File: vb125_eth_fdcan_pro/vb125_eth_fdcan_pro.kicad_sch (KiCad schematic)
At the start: 0 parts

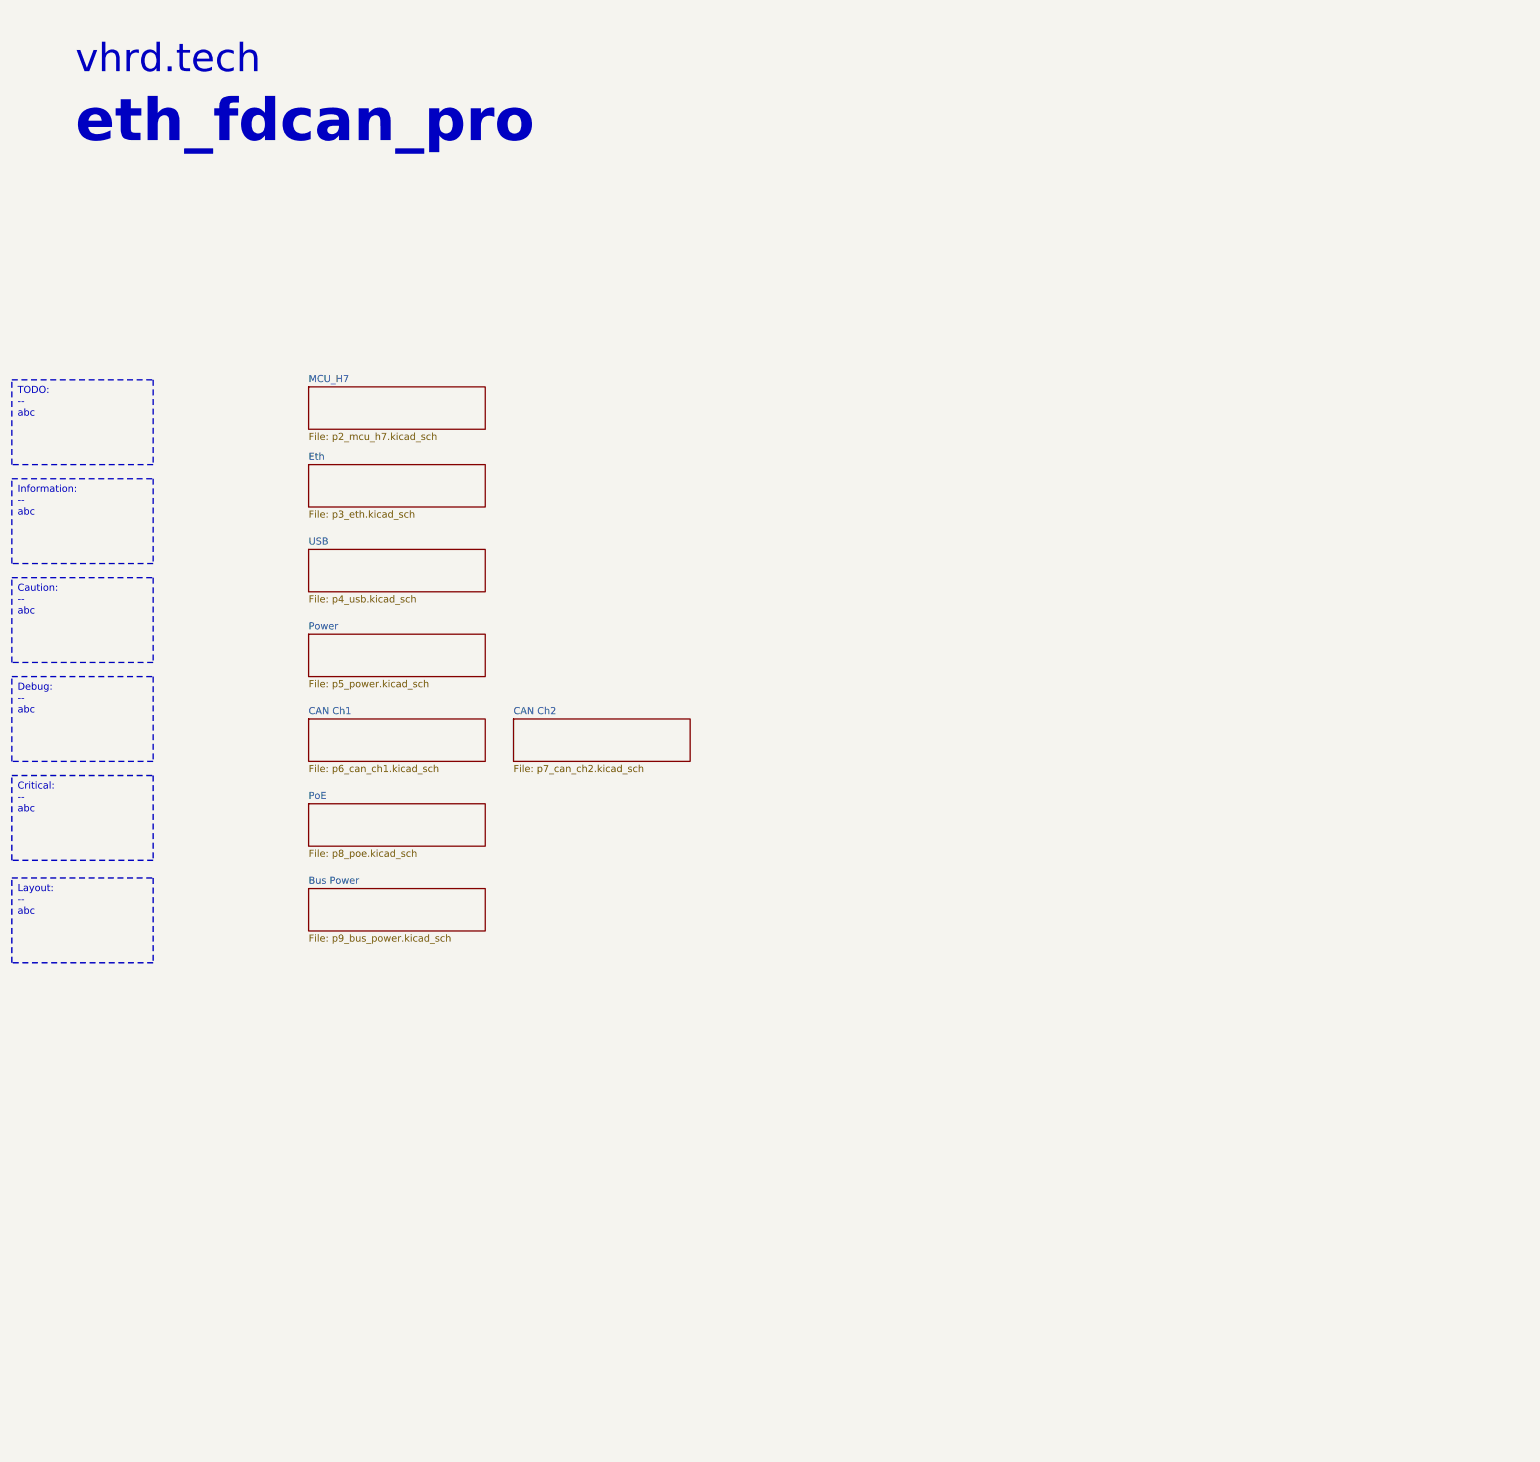
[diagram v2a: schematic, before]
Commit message: CAN schematics. Assign IO on H7.
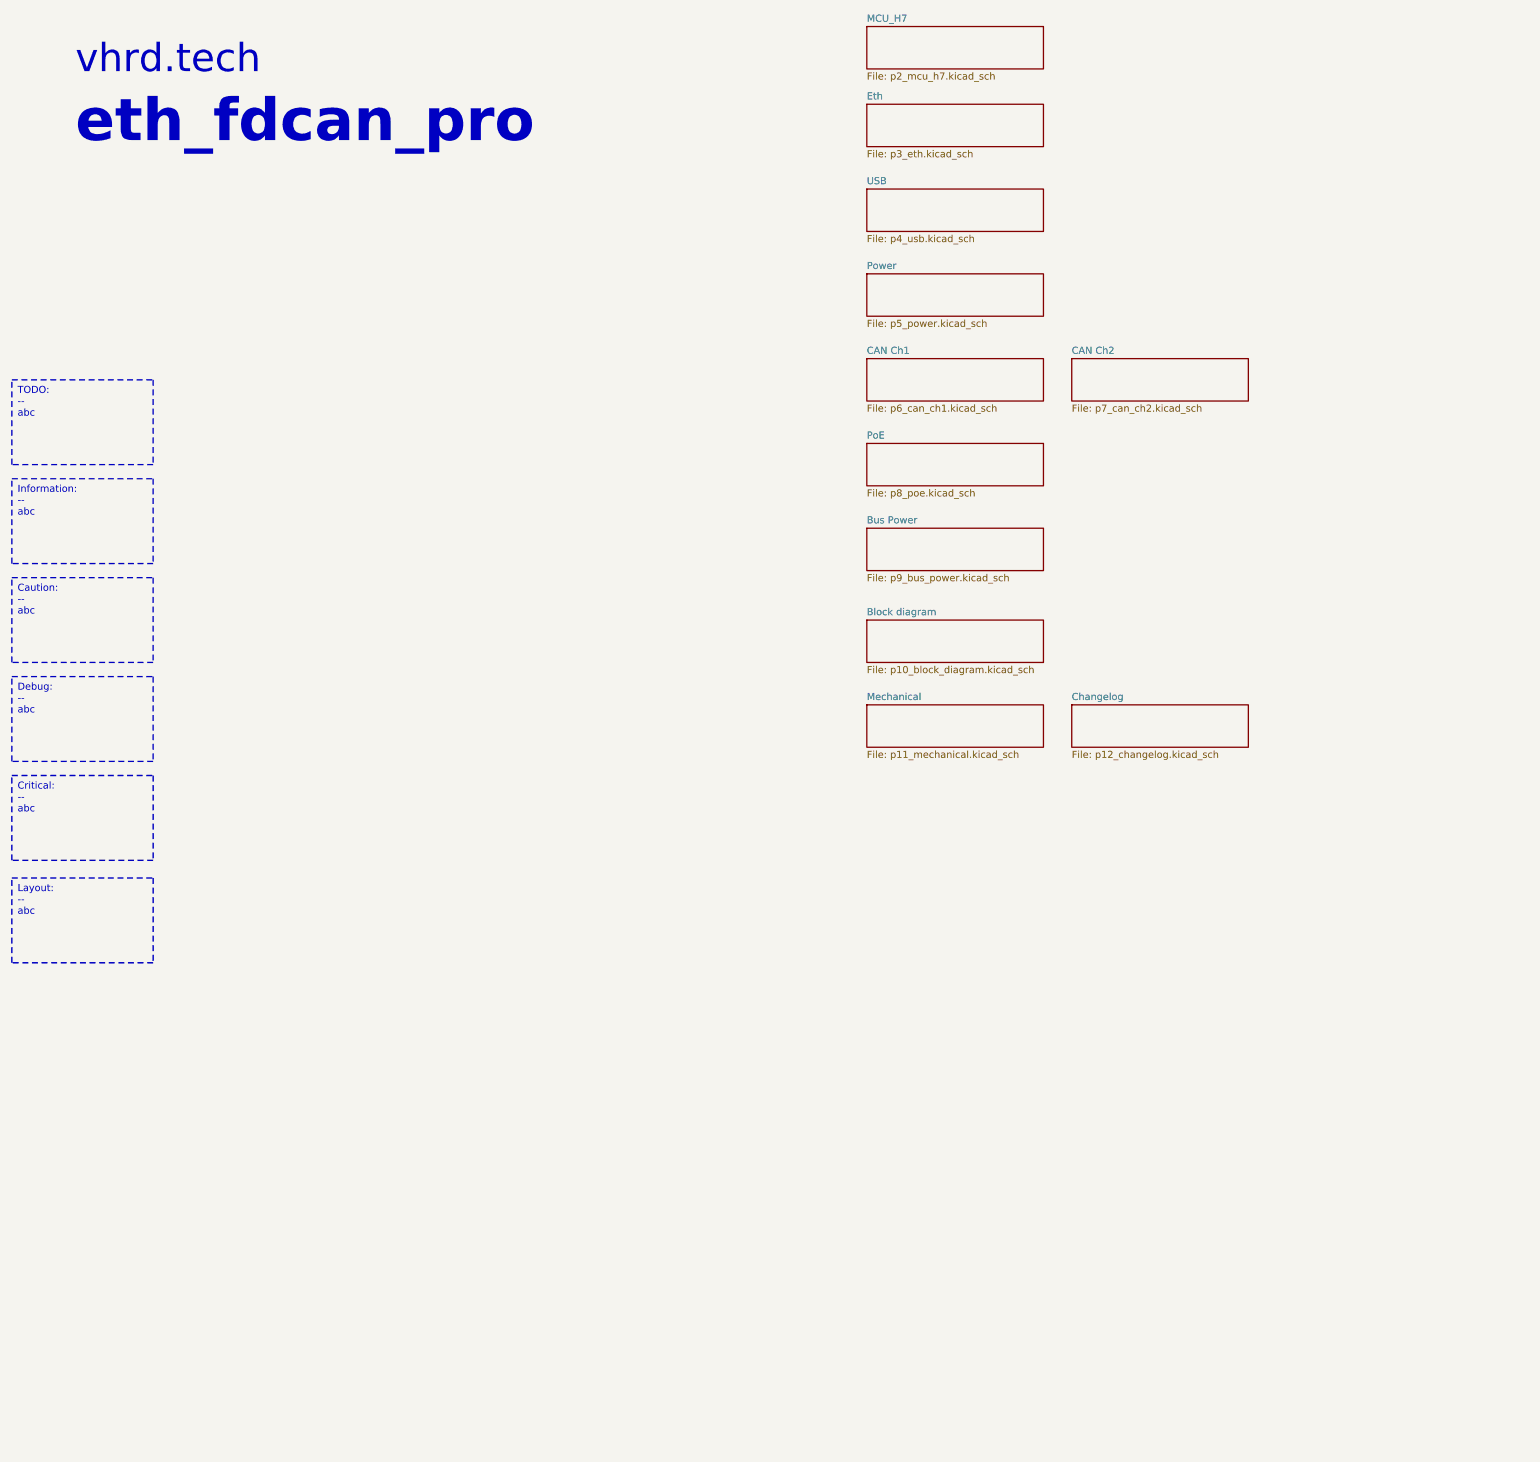
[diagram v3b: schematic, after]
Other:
- added sheet Block diagram (p10_block_diagram.kicad_sch)
- added sheet Changelog (p12_changelog.kicad_sch)
- added sheet Mechanical (p11_mechanical.kicad_sch)
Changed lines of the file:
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@@
     (effects (font (face "Orbitron") (size 5.08 5.08) (color 0 0 0 1)) (justify left bottom))
   )
-  (sheet (at 69.85 119.38) (size 31.75 7.62) (fields_autoplaced)
+  (sheet (at 170.18 54.61) (size 31.75 7.62) (fields_autoplaced)
     (stroke (width 0.1524) (type solid))
     (fill (color 0 0 0 0.0000))
-    (property "Sheetname" "USB" (at 69.85 118.6684 0)
+    (property "Sheetname" "USB" (at 170.18 53.8984 0)
       (effects (font (size 1.27 1.27)) (justify left bottom))
     )
-    (property "Sheetfile" "p4_usb.kicad_sch" (at 69.85 127.5846 0)
+    (property "Sheetfile" "p4_usb.kicad_sch" (at 170.18 62.8146 0)
       (effects (font (size 1.27 1.27)) (justify left top))
     )
@@
     )
   )
-  (sheet (at 69.85 180.34) (size 31.75 7.62) (fields_autoplaced)
+  (sheet (at 170.18 115.57) (size 31.75 7.62) (fields_autoplaced)
     (stroke (width 0.1524) (type solid))
     (fill (color 0 0 0 0.0000))
-    (property "Sheetname" "Bus Power" (at 69.85 179.6284 0)
+    (property "Sheetname" "Bus Power" (at 170.18 114.8584 0)
       (effects (font (size 1.27 1.27)) (justify left bottom))
     )
-    (property "Sheetfile" "p9_bus_power.kicad_sch" (at 69.85 188.5446 0)
+    (property "Sheetfile" "p9_bus_power.kicad_sch" (at 170.18 123.7746 0)
       (effects (font (size 1.27 1.27)) (justify left top))
     )
@@
     )
   )
-  (sheet (at 69.85 134.62) (size 31.75 7.62) (fields_autoplaced)
+  (sheet (at 170.18 147.32) (size 31.75 7.62) (fields_autoplaced)
     (stroke (width 0.1524) (type solid))
     (fill (color 0 0 0 0.0000))
-    (property "Sheetname" "Power" (at 69.85 133.9084 0)
+    (property "Sheetname" "Mechanical" (at 170.18 146.6084 0)
       (effects (font (size 1.27 1.27)) (justify left bottom))
     )
-    (property "Sheetfile" "p5_power.kicad_sch" (at 69.85 142.8246 0)
+    (property "Sheetfile" "p11_mechanical.kicad_sch" (at 170.18 155.5246 0)
+      (effects (font (size 1.27 1.27)) (justify left top))
+    )
+    (instances
+      (project "vb125_eth_fdcan_pro"
+        (path "/b473bccb-f14c-41d5-b473-137d3ef8ae1e" (page "11"))
+      )
+    )
+  )
+  (sheet (at 170.18 132.08) (size 31.75 7.62) (fields_autoplaced)
+    (stroke (width 0.1524) (type solid))
+    (fill (color 0 0 0 0.0000))
+    (property "Sheetname" "Block diagram" (at 170.18 131.3684 0)
+      (effects (font (size 1.27 1.27)) (justify left bottom))
+    )
+    (property "Sheetfile" "p10_block_diagram.kicad_sch" (at 170.18 140.2846 0)
+      (effects (font (size 1.27 1.27)) (justify left top))
+    )
+    (instances
+      (project "vb125_eth_fdcan_pro"
+        (path "/b473bccb-f14c-41d5-b473-137d3ef8ae1e" (page "10"))
+      )
+    )
+  )
+  (sheet (at 170.18 69.85) (size 31.75 7.62) (fields_autoplaced)
+    (stroke (width 0.1524) (type solid))
+    (fill (color 0 0 0 0.0000))
+    (property "Sheetname" "Power" (at 170.18 69.1384 0)
+      (effects (font (size 1.27 1.27)) (justify left bottom))
+    )
+    (property "Sheetfile" "p5_power.kicad_sch" (at 170.18 78.0546 0)
       (effects (font (size 1.27 1.27)) (justify left top))
     )
@@
     )
   )
-  (sheet (at 69.85 165.1) (size 31.75 7.62) (fields_autoplaced)
+  (sheet (at 170.18 100.33) (size 31.75 7.62) (fields_autoplaced)
     (stroke (width 0.1524) (type solid))
     (fill (color 0 0 0 0.0000))
-    (property "Sheetname" "PoE" (at 69.85 164.3884 0)
+    (property "Sheetname" "PoE" (at 170.18 99.6184 0)
       (effects (font (size 1.27 1.27)) (justify left bottom))
     )
-    (property "Sheetfile" "p8_poe.kicad_sch" (at 69.85 173.3046 0)
+    (property "Sheetfile" "p8_poe.kicad_sch" (at 170.18 108.5346 0)
       (effects (font (size 1.27 1.27)) (justify left top))
     )
@@
     )
   )
-  (sheet (at 69.85 104.14) (size 31.75 7.62) (fields_autoplaced)
+  (sheet (at 170.18 39.37) (size 31.75 7.62) (fields_autoplaced)
     (stroke (width 0.1524) (type solid))
     (fill (color 0 0 0 0.0000))
-    (property "Sheetname" "Eth" (at 69.85 103.4284 0)
+    (property "Sheetname" "Eth" (at 170.18 38.6584 0)
       (effects (font (size 1.27 1.27)) (justify left bottom))
     )
-    (property "Sheetfile" "p3_eth.kicad_sch" (at 69.85 112.3446 0)
+    (property "Sheetfile" "p3_eth.kicad_sch" (at 170.18 47.5746 0)
       (effects (font (size 1.27 1.27)) (justify left top))
     )
@@
     )
   )
-  (sheet (at 69.85 149.86) (size 31.75 7.62) (fields_autoplaced)
+  (sheet (at 170.18 85.09) (size 31.75 7.62) (fields_autoplaced)
     (stroke (width 0.1524) (type solid))
     (fill (color 0 0 0 0.0000))
-    (property "Sheetname" "CAN Ch1" (at 69.85 149.1484 0)
+    (property "Sheetname" "CAN Ch1" (at 170.18 84.3784 0)
       (effects (font (size 1.27 1.27)) (justify left bottom))
     )
-    (property "Sheetfile" "p6_can_ch1.kicad_sch" (at 69.85 158.0646 0)
+    (property "Sheetfile" "p6_can_ch1.kicad_sch" (at 170.18 93.2946 0)
       (effects (font (size 1.27 1.27)) (justify left top))
     )
@@
     )
   )
-  (sheet (at 69.85 90.17) (size 31.75 7.62) (fields_autoplaced)
+  (sheet (at 207.01 147.32) (size 31.75 7.62) (fields_autoplaced)
     (stroke (width 0.1524) (type solid))
     (fill (color 0 0 0 0.0000))
-    (property "Sheetname" "MCU_H7" (at 69.85 89.4584 0)
+    (property "Sheetname" "Changelog" (at 207.01 146.6084 0)
       (effects (font (size 1.27 1.27)) (justify left bottom))
     )
-    (property "Sheetfile" "p2_mcu_h7.kicad_sch" (at 69.85 98.3746 0)
+    (property "Sheetfile" "p12_changelog.kicad_sch" (at 207.01 155.5246 0)
+      (effects (font (size 1.27 1.27)) (justify left top))
+    )
+    (instances
+      (project "vb125_eth_fdcan_pro"
+        (path "/b473bccb-f14c-41d5-b473-137d3ef8ae1e" (page "12"))
+      )
+    )
+  )
+  (sheet (at 170.18 25.4) (size 31.75 7.62) (fields_autoplaced)
+    (stroke (width 0.1524) (type solid))
+    (fill (color 0 0 0 0.0000))
+    (property "Sheetname" "MCU_H7" (at 170.18 24.6884 0)
+      (effects (font (size 1.27 1.27)) (justify left bottom))
+    )
+    (property "Sheetfile" "p2_mcu_h7.kicad_sch" (at 170.18 33.6046 0)
       (effects (font (size 1.27 1.27)) (justify left top))
     )
@@
     )
   )
-  (sheet (at 106.68 149.86) (size 31.75 7.62) (fields_autoplaced)
+  (sheet (at 207.01 85.09) (size 31.75 7.62) (fields_autoplaced)
     (stroke (width 0.1524) (type solid))
     (fill (color 0 0 0 0.0000))
-    (property "Sheetname" "CAN Ch2" (at 106.68 149.1484 0)
+    (property "Sheetname" "CAN Ch2" (at 207.01 84.3784 0)
       (effects (font (size 1.27 1.27)) (justify left bottom))
     )
-    (property "Sheetfile" "p7_can_ch2.kicad_sch" (at 106.68 158.0646 0)
+    (property "Sheetfile" "p7_can_ch2.kicad_sch" (at 207.01 93.2946 0)
       (effects (font (size 1.27 1.27)) (justify left top))
     )
